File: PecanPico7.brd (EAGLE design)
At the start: 34.2 x 50 mm, 178 parts, among them IC1 Si4060-B1B-FM, IC10 TPS62260DRVT, IC11 TPS62261DRVT, IC12 TPS63021, IC13 RF6886, IC14 TPS78227DDCR, IC16 PAC1720-1-AIA-TR, IC2 Si4060-B1B-FM, IC3 BME280_BME280, IC4 uBlox MAX7/8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

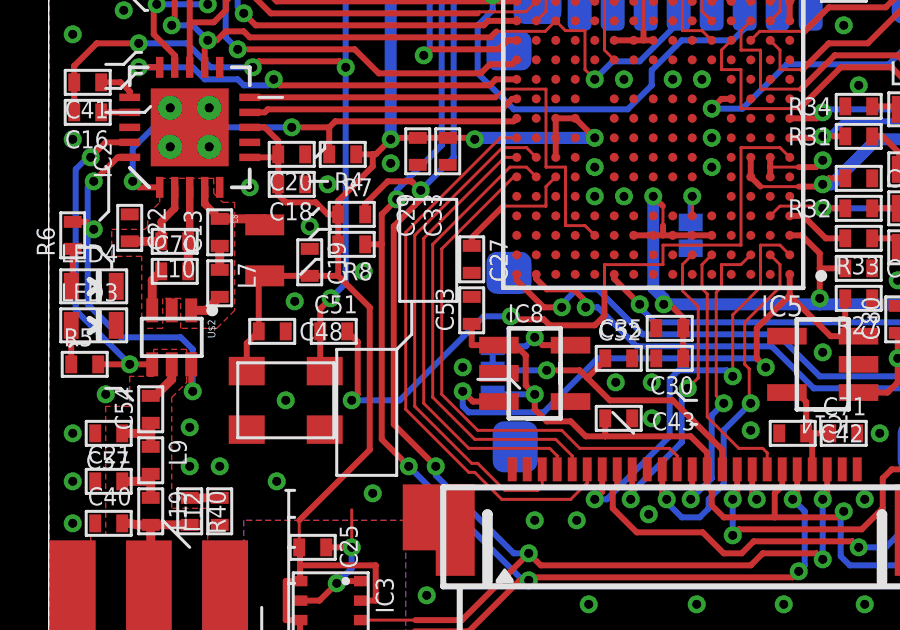
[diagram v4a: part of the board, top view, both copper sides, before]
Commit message: Moved parts around
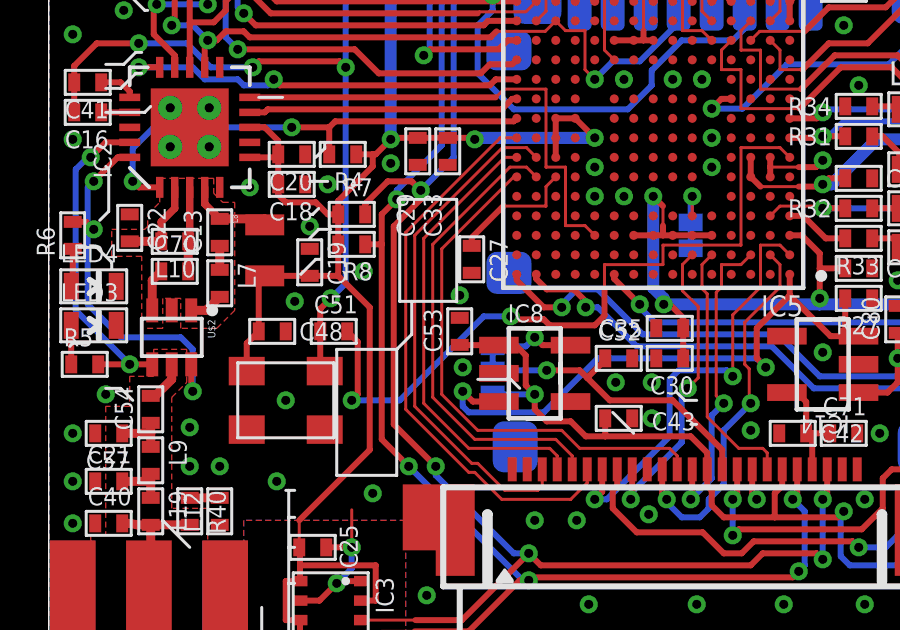
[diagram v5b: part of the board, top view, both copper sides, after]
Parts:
- moved C53 0.81 mm to (13.7, 11.1)
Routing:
- net GND: vias 128 -> 129
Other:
- board text removed: "XIN"
- board text removed: "XOUT"
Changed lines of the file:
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@@
 <text x="14.3" y="13.5" size="0.7" layer="38" rot="MR270">1.3V</text>
 <text x="14.3" y="8.4" size="0.7" layer="38" rot="MR270">1.8V</text>
-<text x="-4.1" y="21.5" size="0.7" layer="38" rot="MR180">XIN</text>
-<text x="-5" y="22.9" size="0.7" layer="38" rot="MR180">XOUT</text>
-<text x="-3.8" y="18.5" size="0.7" layer="38" rot="MR180">XIN</text>
-<text x="-4.9" y="19.8" size="0.7" layer="38" rot="MR180">XOUT</text>
 <wire x1="23.6" y1="46.8" x2="23.6" y2="43.8" width="0.2" layer="38"/>
 <wire x1="23.6" y1="43.8" x2="22.8" y2="43" width="0.2" layer="38"/>
@@
 <element name="SJ4" library="PecanPico6" package="SJ_2" value="" x="14.8" y="9.8" rot="MR270"/>
 <element name="C52" library="PecanPico6" package="0402" value="100nF" x="19" y="10.2"/>
-<element name="C53" library="PecanPico6" package="0402" value="100nF" x="14.1" y="11.8" rot="R90"/>
+<element name="C53" library="PecanPico6" package="0402" value="100nF" x="13.7" y="11.1" rot="R90"/>
 <element name="R38" library="PecanPico6" package="0402" value="1k" x="1.3" y="32.3"/>
 <element name="L6" library="PecanPico6" package="0402" value="30nH" x="6.3" y="32.7" rot="R90"/>
@@
 <via x="0.8" y="24.6" extent="1-16" drill="0.3"/>
 <via x="2.5" y="21.8" extent="1-16" drill="0.3"/>
+<via x="13.7" y="12.3" extent="1-16" drill="0.3"/>
 </signal>
 <signal name="N$5">
@@
 <wire x1="25.7" y1="13.2" x2="25.7" y2="12.2" width="0.2" layer="1"/>
 <wire x1="26.55" y1="13.2" x2="25.7" y2="13.2" width="0.2" layer="1"/>
-<wire x1="14.1" y1="11.35" x2="14.1" y2="10.6398" width="0.2" layer="1"/>
+<wire x1="13.7" y1="10.65" x2="14.1" y2="10.6398" width="0.2" layer="1"/>
 <wire x1="14.1" y1="10.6398" x2="15.0062" y2="10.6398" width="0.2" layer="1"/>
 <wire x1="16.2" y1="9" x2="14.8" y2="9" width="0.2" layer="16"/>

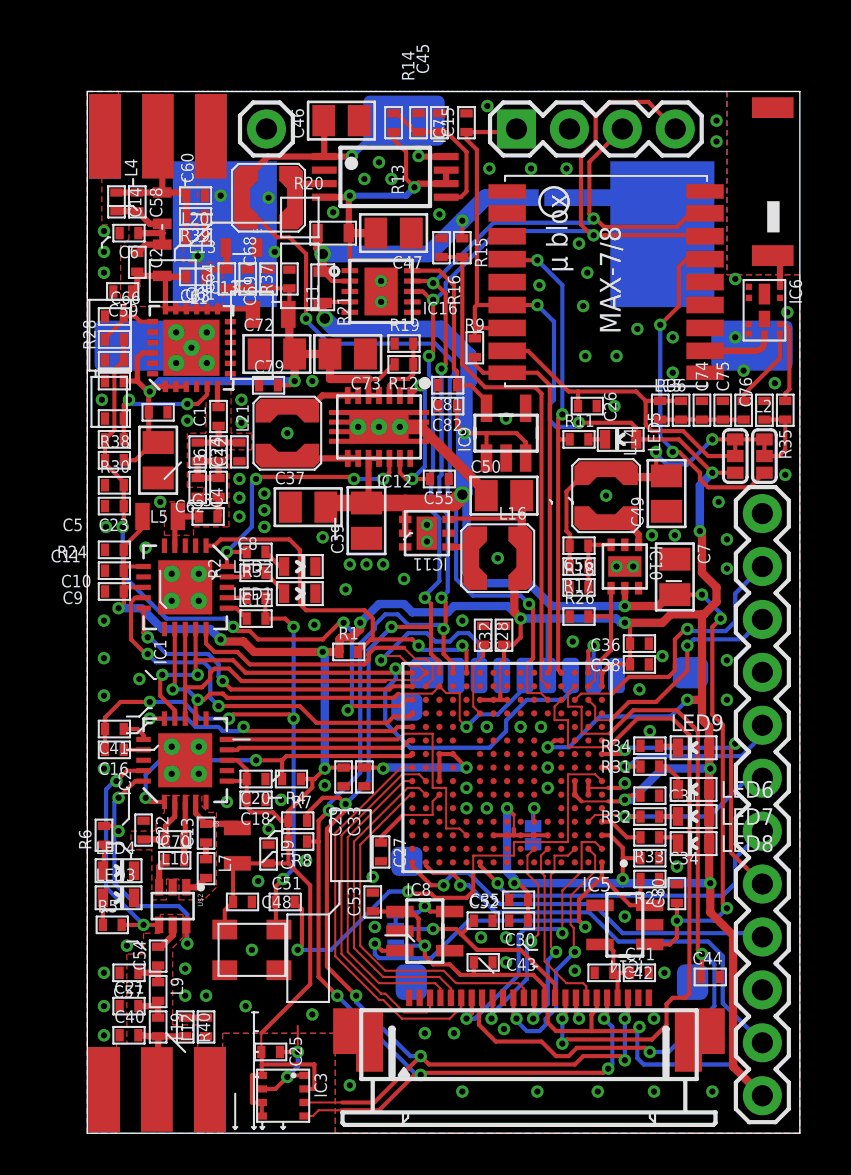
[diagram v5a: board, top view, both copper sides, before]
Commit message: Modified voltage supply of camera
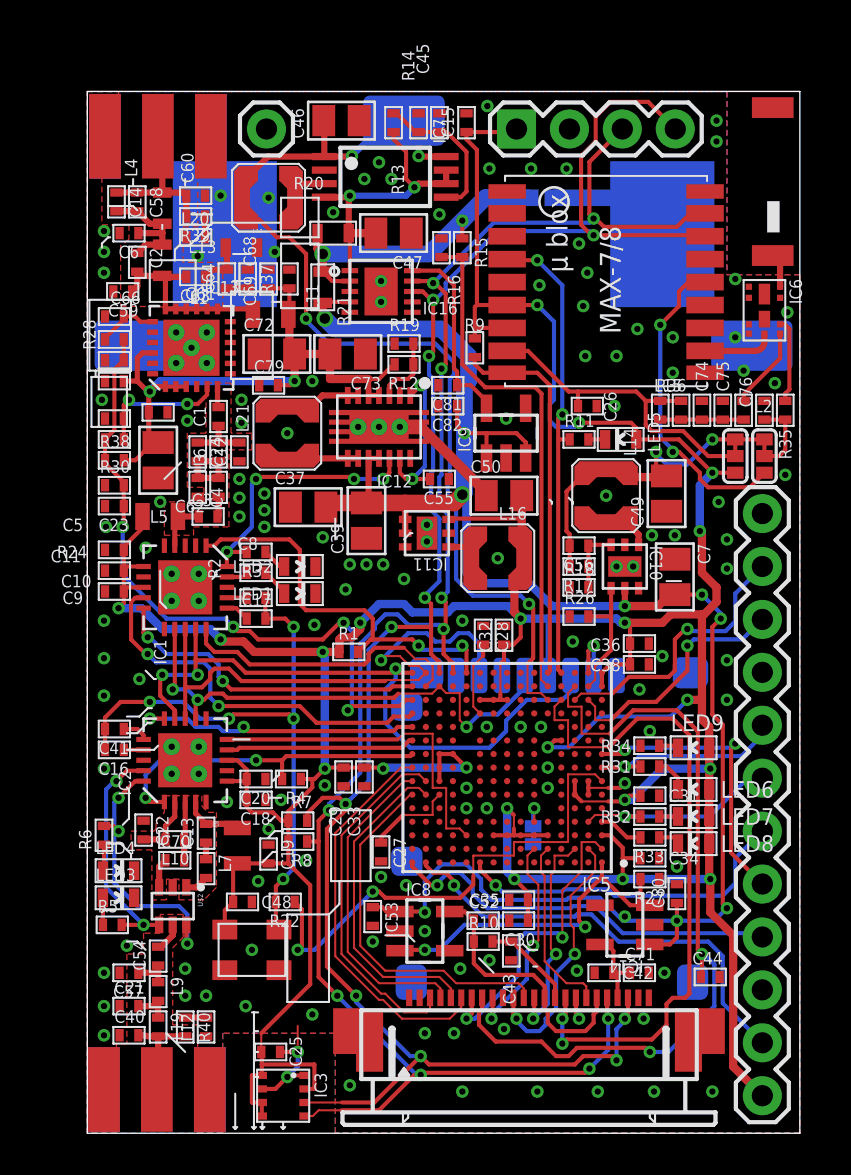
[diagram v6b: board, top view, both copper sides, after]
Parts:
- removed SJ4: (no value), PecanPico6:SJ_2
- added R10: DIODE, PecanPico6:0402
- IC8: value LP5951MF-1.3/NOPB -> TI TC1185-1.8VCT713
- R22: value 100pF -> 10k
- moved C43 1.46 mm to (20.4, 8.75), turned to 270 degrees
- moved C53 0.70 mm to (13.7, 10.4), turned to 270 degrees
- turned R22 to 180 degrees
- renumbered C51 to R22
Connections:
- removed net N$57: IC8.5, SJ4.1
- new net N$12: C43.P$1, R10.P$2, X1.15
- net CAM_VCC_CORE: now also IC8.5, R10.P$1, X1.14, X1.19; no longer SJ4.2, X1.15
- net CLOCK: now also R22.P$2; no longer R22.P$1
- net N$39: now also R22.P$1; no longer R22.P$2
- net N$54: now also IC4.14_VCC_RF; no longer IC4.15_RESERVED
- net VBAT_OUT: now also C53.P$1, IC8.1
- net VCC: no longer C43.P$1, C53.P$1, IC8.1, SJ4.3, X1.14, X1.19
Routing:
- net VCC: track 250.9 -> 221.6 mm, vias 23 -> 21
- net VBAT_OUT: track 72.6 -> 90.6 mm, vias 8 -> 9
- net N$12: track 0.00 -> 4.50 mm
- net CAM_EN: track 21.1 -> 17.7 mm
- net N$57: track 2.83 -> 0.00 mm, vias 1 -> 0
- net CAM_VCC_CORE: track 10.3 -> 12.8 mm, vias 1 -> 0
- net N$54: track 16.5 -> 15.3 mm
- net I2C_SCL: track 89.0 -> 88.2 mm
- net GND: vias 129 -> 130

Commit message: Added Polygons for MCU
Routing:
- net GND: vias 130 -> 131
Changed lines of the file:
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@@
 <contactref element="C75" pad="P$1"/>
 <contactref element="C76" pad="P$1"/>
-<polygon width="0.1" layer="16">
+<polygon width="0.2" layer="16">
 <vertex x="0" y="50"/>
 <vertex x="30.7" y="50"/>
@@
 <vertex x="0" y="0"/>
 </polygon>
-<polygon width="0.1" layer="1">
+<polygon width="0.2" layer="1">
 <vertex x="0" y="50"/>
 <vertex x="1.5" y="50"/>
-<vertex x="1.5" y="45.9"/>
-<vertex x="0.7" y="45.9"/>
-<vertex x="0.7" y="43.6"/>
-<vertex x="2" y="43.6"/>
-<vertex x="2" y="42.9"/>
-<vertex x="1.6" y="42.6"/>
-<vertex x="1.6" y="39.7"/>
-<vertex x="6.5" y="39.6"/>
-<vertex x="6.5" y="41.8"/>
-<vertex x="4.6" y="41.8"/>
-<vertex x="4.6" y="43.5"/>
-<vertex x="5.3" y="43.5"/>
+<vertex x="1.5" y="45.5"/>
+<vertex x="5.3" y="45.5"/>
 <vertex x="5.3" y="50"/>
 <vertex x="30.7" y="50"/>
@@
 <vertex x="6.5" y="0"/>
 <vertex x="5.3" y="0"/>
-<vertex x="5.3" y="5.2"/>
-<vertex x="4.1" y="5.2"/>
-<vertex x="4.1" y="8.9"/>
-<vertex x="4.6" y="9.4"/>
-<vertex x="4.6" y="10.5"/>
-<vertex x="3.5" y="10.5"/>
-<vertex x="3.5" y="9.6"/>
-<vertex x="2.7" y="9.6"/>
-<vertex x="2.7" y="8.6"/>
-<vertex x="1.9" y="8.6"/>
-<vertex x="1.9" y="4.3"/>
+<vertex x="5.3" y="4.3"/>
 <vertex x="1.4" y="4.3"/>
 <vertex x="1.4" y="0"/>
@@
 <wire x1="4.05" y1="26.85" x2="4.7" y2="26.2" width="0.2" layer="1"/>
 <via x="27" y="19.3" extent="1-16" drill="0.3"/>
-<via x="28.3" y="12.8" extent="1-16" drill="0.3"/>
+<via x="28.3" y="12.9" extent="1-16" drill="0.3"/>
 <via x="23.6" y="42.7" extent="1-16" drill="0.3"/>
 <via x="24" y="41.3" extent="1-16" drill="0.3"/>
@@
 <via x="16.3" y="29.2" extent="1-16" drill="0.3"/>
 <via x="27.7" y="7.7" extent="1-16" drill="0.3"/>
-<via x="25.8" y="10.4" extent="1-16" drill="0.3"/>
+<via x="25.8" y="8.6" extent="1-16" drill="0.3"/>
 <via x="26.7" y="5.5" extent="1-16" drill="0.3"/>
 <via x="13.7" y="9.2" extent="1-16" drill="0.3"/>
@@
 <vertex x="5.7" y="36"/>
 <vertex x="5.7" y="33.6"/>
-</polygon>
-<polygon width="0.2" layer="1" pour="cutout">
-<vertex x="3.1" y="11.2"/>
-<vertex x="3.1" y="13.6"/>
-<vertex x="2.1" y="13.6"/>
-<vertex x="2.1" y="14.5"/>
-<vertex x="3.2" y="14.5"/>
-<vertex x="3.3" y="14.6"/>
-<vertex x="3.3" y="15"/>
-<vertex x="3.7" y="15.4"/>
-<vertex x="3.7" y="16.2"/>
-<vertex x="5.5" y="16.2"/>
-<vertex x="5.5" y="15.7"/>
-<vertex x="5.8" y="15.4"/>
-<vertex x="6.2" y="15.4"/>
-<vertex x="6.2" y="11.8"/>
-<vertex x="5.6" y="11.2"/>
-<vertex x="4.4" y="11.2"/>
-<vertex x="4.4" y="12.2"/>
-<vertex x="3.8" y="12.2"/>
-<vertex x="3.8" y="11.2"/>
 </polygon>
 <via x="10.5" y="13.1" extent="1-16" drill="0.3"/>
@@
 <via x="14.1" y="12.3" extent="1-16" drill="0.3"/>
 <via x="19.3" y="8.3" extent="1-16" drill="0.3"/>
-<via x="15.3" y="11.9" extent="1-16" drill="0.3"/>
+<via x="15.3" y="11.8" extent="1-16" drill="0.3"/>
 <via x="17.9" y="7.9" extent="1-16" drill="0.3"/>
+<polygon width="0.1" layer="1">
+<vertex x="15.1" y="22.6"/>
+<vertex x="25.2" y="22.6"/>
+<vertex x="25.2" y="13.1"/>
+<vertex x="25.2" y="12.5"/>
+<vertex x="15.5" y="12.5"/>
+<vertex x="15.1" y="12.5"/>
+</polygon>
+<via x="3" y="39.8" extent="1-16" drill="0.3"/>
+<wire x1="19.45" y1="10.2" x2="19.3" y2="8.3" width="0" layer="19" extent="1-1"/>
 </signal>
 <signal name="N$5">
@@
 <wire x1="20.8" y1="24.7" x2="22.1" y2="24.7" width="0.4" layer="16"/>
 <wire x1="22.1" y1="24.7" x2="25.4" y2="24.7" width="0.4" layer="16"/>
-<wire x1="31" y1="9.5" x2="31" y2="3.2" width="0.4" layer="1"/>
+<wire x1="31" y1="8.2" x2="31" y2="3.2" width="0.4" layer="1"/>
 <wire x1="31" y1="3.2" x2="32.4" y2="1.8" width="0.4" layer="1"/>
-<wire x1="29.9" y1="12.2" x2="29.9" y2="10.6" width="0.4" layer="1"/>
+<wire x1="29.9" y1="12.2" x2="29.9" y2="9.3" width="0.4" layer="1"/>
 <wire x1="8.375" y1="1.475" x2="8.375" y2="0.825" width="0.2" layer="1"/>
 <via x="14.2" y="17.5" extent="1-16" drill="0.3"/>
@@
 <wire x1="25.7" y1="13.2" x2="25.7" y2="12.2" width="0.2" layer="1"/>
 <wire x1="26.55" y1="13.2" x2="25.7" y2="13.2" width="0.2" layer="1"/>
-<wire x1="29.9" y1="10.6" x2="31" y2="9.5" width="0.4" layer="1"/>
+<wire x1="29.9" y1="9.3" x2="31" y2="8.2" width="0.4" layer="1"/>
 <wire x1="9.65" y1="14" x2="9.65" y2="12.95" width="0.2" layer="1"/>
 <wire x1="28" y1="20" x2="24.6" y2="20" width="0.2" layer="16"/>
@@
 <wire x1="10.1" y1="8.8" x2="10.3" y2="9" width="0.2" layer="1"/>
 <wire x1="10.3" y1="9" x2="10.3" y2="10.75" width="0.2" layer="1"/>
-<wire x1="13.7" y1="11.6" x2="14" y2="11.6" width="0.2" layer="1"/>
-<wire x1="14" y1="11.6" x2="14.3" y2="11.3" width="0.2" layer="1"/>
-<wire x1="14.3" y1="11.3" x2="17.9" y2="11.3" width="0.2" layer="1"/>
-<wire x1="17.9" y1="11.3" x2="18.525" y2="11.925" width="0.2" layer="1"/>
+<wire x1="13.7" y1="11.6" x2="14.1" y2="11.6" width="0.2" layer="1"/>
+<wire x1="14.1" y1="11.6" x2="14.5" y2="11.2" width="0.2" layer="1"/>
+<wire x1="14.5" y1="11.2" x2="17.8" y2="11.2" width="0.2" layer="1"/>
+<wire x1="17.8" y1="11.2" x2="18.525" y2="11.925" width="0.2" layer="1"/>
 <wire x1="18.525" y1="11.925" x2="18.525" y2="12.35" width="0.2" layer="1"/>
 <wire x1="18.525" y1="12.35" x2="18.525" y2="13.325" width="0.1" layer="1"/>
@@
 <wire x1="30" y1="24.3" x2="30" y2="20.1" width="0.2" layer="1"/>
 <wire x1="30" y1="20.1" x2="30.5" y2="19.6" width="0.2" layer="1"/>
-<wire x1="30.5" y1="19.6" x2="30.5" y2="11" width="0.2" layer="1"/>
-<wire x1="30.5" y1="11" x2="30.7" y2="10.8" width="0.2" layer="1"/>
-<via x="30.7" y="10.8" extent="1-16" drill="0.3"/>
-<wire x1="30.7" y1="10.8" x2="30.1" y2="10.2" width="0.2" layer="16"/>
-<wire x1="30.1" y1="10.2" x2="28.3" y2="10.2" width="0.2" layer="16"/>
+<wire x1="30.5" y1="19.6" x2="30.5" y2="10.3" width="0.2" layer="1"/>
+<wire x1="30.5" y1="10.3" x2="30.6" y2="10.2" width="0.2" layer="1"/>
+<via x="30.6" y="10.2" extent="1-16" drill="0.3"/>
+<wire x1="30.6" y1="10.2" x2="28.3" y2="10.2" width="0.2" layer="16"/>
 <via x="28.3" y="10.2" extent="1-16" drill="0.3"/>
 <wire x1="17.75" y1="34.9" x2="17.75" y2="33.95" width="0.2" layer="1"/>
@@
 <contactref element="X1" pad="21"/>
 <contactref element="C42" pad="P$1"/>
-<wire x1="24.6062" y1="9.0602" x2="24.9398" y2="9.0602" width="0.2" layer="1"/>
-<wire x1="24.9398" y1="9.0602" x2="25.25" y2="8.75" width="0.2" layer="1"/>
-<wire x1="25.25" y1="8.75" x2="25.25" y2="7.7" width="0.2" layer="1"/>
 <wire x1="25.45" y1="7.7" x2="26.05" y2="7.7" width="0.2" layer="1"/>
 <wire x1="25.25" y1="7.7" x2="25.45" y2="7.7" width="0.2" layer="1"/>
 <wire x1="25.45" y1="7.7" x2="25.45" y2="6.5" width="0.2" layer="1"/>
+<wire x1="25.25" y1="7.7" x2="25.25" y2="8.15" width="0.2" layer="1"/>
+<wire x1="25.25" y1="8.15" x2="24.6062" y2="8.7938" width="0.2" layer="1"/>
+<wire x1="24.6062" y1="8.7938" x2="24.6062" y2="9.0602" width="0.2" layer="1"/>
 </signal>
 <signal name="N$13">
